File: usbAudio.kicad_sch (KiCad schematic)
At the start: 35 parts, among them J1 USB_B_Micro, J2 54-00176, U1 PCM2906CDBR, U2 MAX9814, U3 TCR2EF36, Y1 12MHz

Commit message: Update design and readme
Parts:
- removed C6: 1uF, Capacitor_SMD:C_0603_1608Metric_Pad1.08x0.95mm_HandSolder, symbol Device:C_Small
- removed D1: D_Schottky_Small, Diode_SMD:D_SOD-523, symbol Device:D_Schottky_Small
- removed JP1: Jumper_NC_Small, Jumper:SolderJumper-2_P1.3mm_Bridged_RoundedPad1.0x1.5mm, symbol Device:Jumper_NC_Small
- removed JP4: Jumper_NO_Small, Jumper:SolderJumper-2_P1.3mm_Open_RoundedPad1.0x1.5mm, symbol Device:Jumper_NO_Small
- removed R7: 13k, Resistor_SMD:R_0603_1608Metric_Pad0.98x0.95mm_HandSolder, symbol Device:R_Small_US
- removed R8: 27k, Resistor_SMD:R_0603_1608Metric_Pad0.98x0.95mm_HandSolder, symbol Device:R_Small_US
- removed U3: TCR2EF36, Package_TO_SOT_SMD:TSOT-23-5, symbol Regulator_Linear:ADP7142AUJZ-3.3
- added C1: 0.1uF, Capacitor_SMD:C_0603_1608Metric_Pad1.08x0.95mm_HandSolder, symbol Device:C_Small
- added C13, C16, C17: 1uF, Capacitor_SMD:C_0603_1608Metric_Pad1.08x0.95mm_HandSolder, symbol Device:C_Small
- added J2: Conn_01x03, Package_TO_SOT_THT:TO-92Flat, symbol Connector_Generic:Conn_01x03
- added U3: TCR2EF36, Package_TO_SOT_SMD:SOT-23-5, symbol Regulator_Linear:MIC5365-3.3YD5
- added U4: MIC5365-3.3YD5, Package_TO_SOT_SMD:SOT-23-5, symbol Regulator_Linear:MIC5365-3.3YD5
- renumbered C13 to C14, C14 to C15, C3 to C2, C8 to C3, C1 to C4, C2 to C6, C4 to C7, C7 to C8, J2 to J3, JP3 to JP1, R3 to R4, R4 to R5, R5 to R6, R2 to R7, R6 to R8
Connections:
- net AMPOUT: now also C1.2
- net GND: now also C13.2, C16.2, C17.2, J2.2 (Pin_2), U3.2 (GND), U4.2 (GND)
- net VBUS: now also C13.1, U3.1 (VIN)
- net VCCCI: now also C16.1, J2.1 (Pin_1), U3.5 (VOUT), U4.1 (VIN)
- net at R8.1, U2.13 (MICBIAS): now also JP2.1; no longer R1.1
- net MICIN: no longer names the net of C2.1, U2.8 (MICIN)
- net MICIN: no longer JP2.1
- net SSPND* renamed *SSPND
- net *SSPND: now also U3.3 (EN), U4.3 (EN)
- new net: C1.1, U1.12 (VINL)
- new net IN_R: J2.3 (Pin_3), U1.13 (VINR)
- new net VBIAS: C17.1, JP2.2, R1.1, U4.5 (VOUT)
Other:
- note added: "Amplifier"
- note added: "Codec"
- note added: "Connectors"
- note added: "Power"
- moved on the sheet: C10, C11, C12, C14, C15, C2, C3, C4, C5, C6, C7, C8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

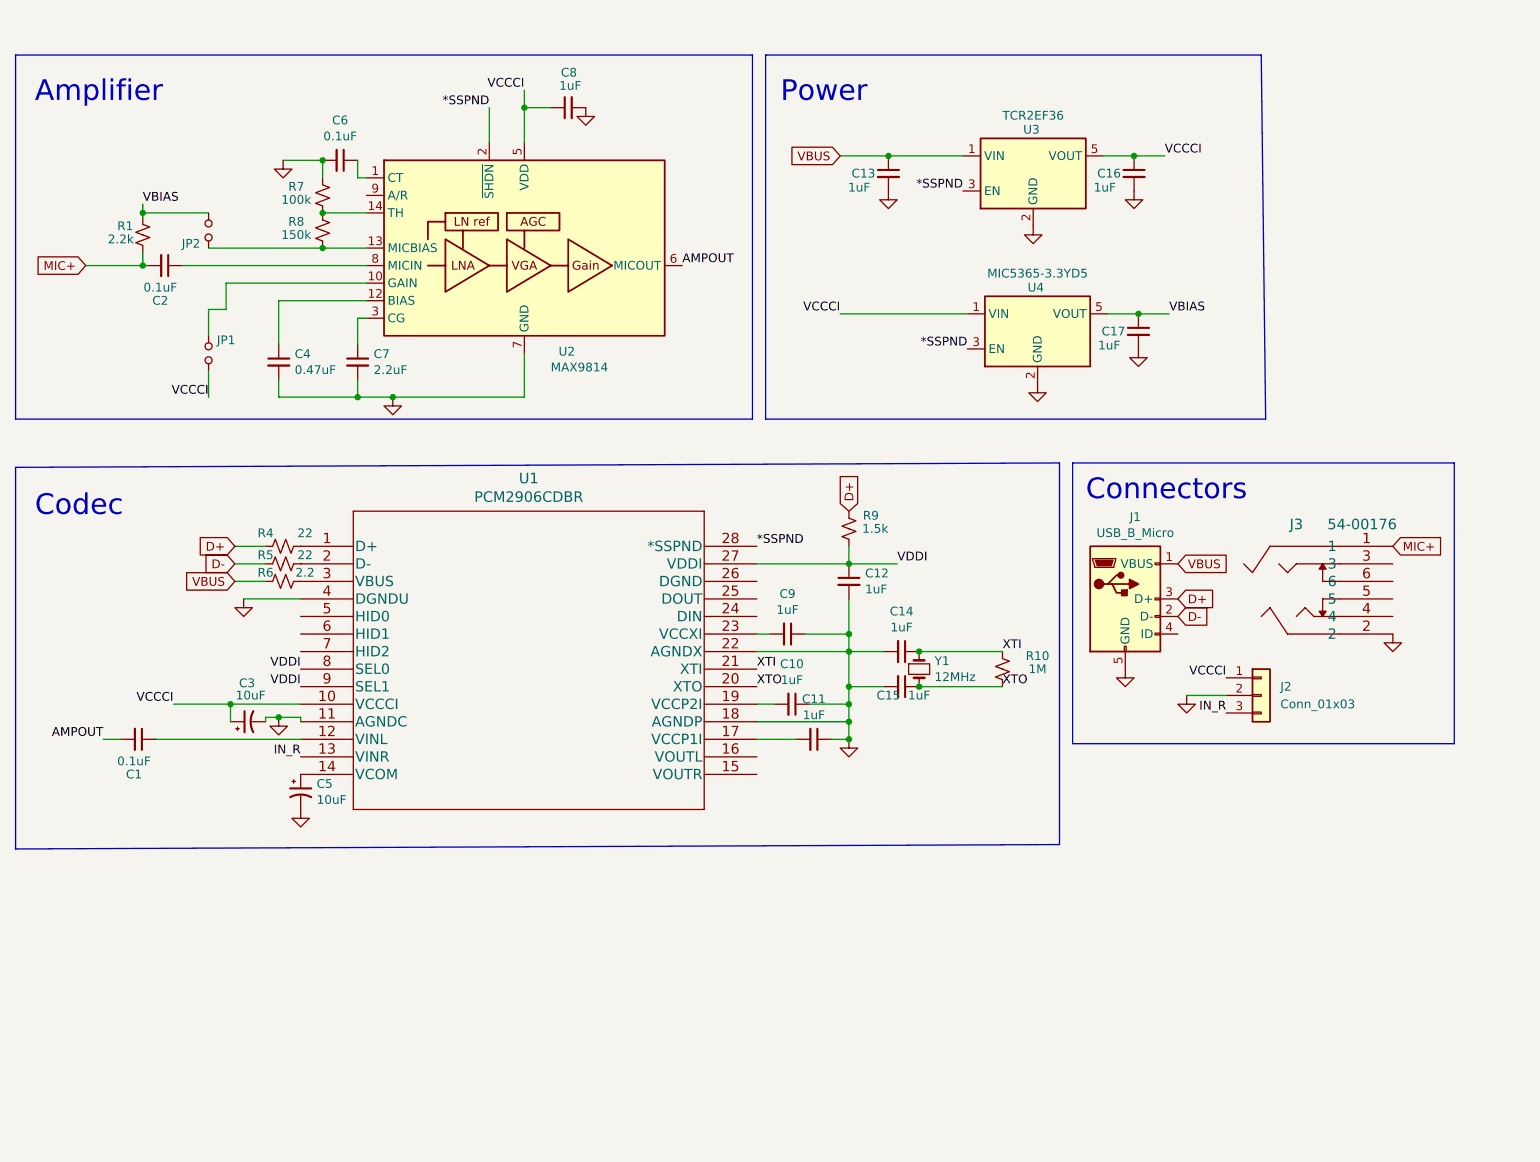
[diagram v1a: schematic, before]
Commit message: Updates from reddit feedback https://www.reddit.com/r/PrintedCircuitBoard/comments/so21cn/project_review_usb_microphone_interface/
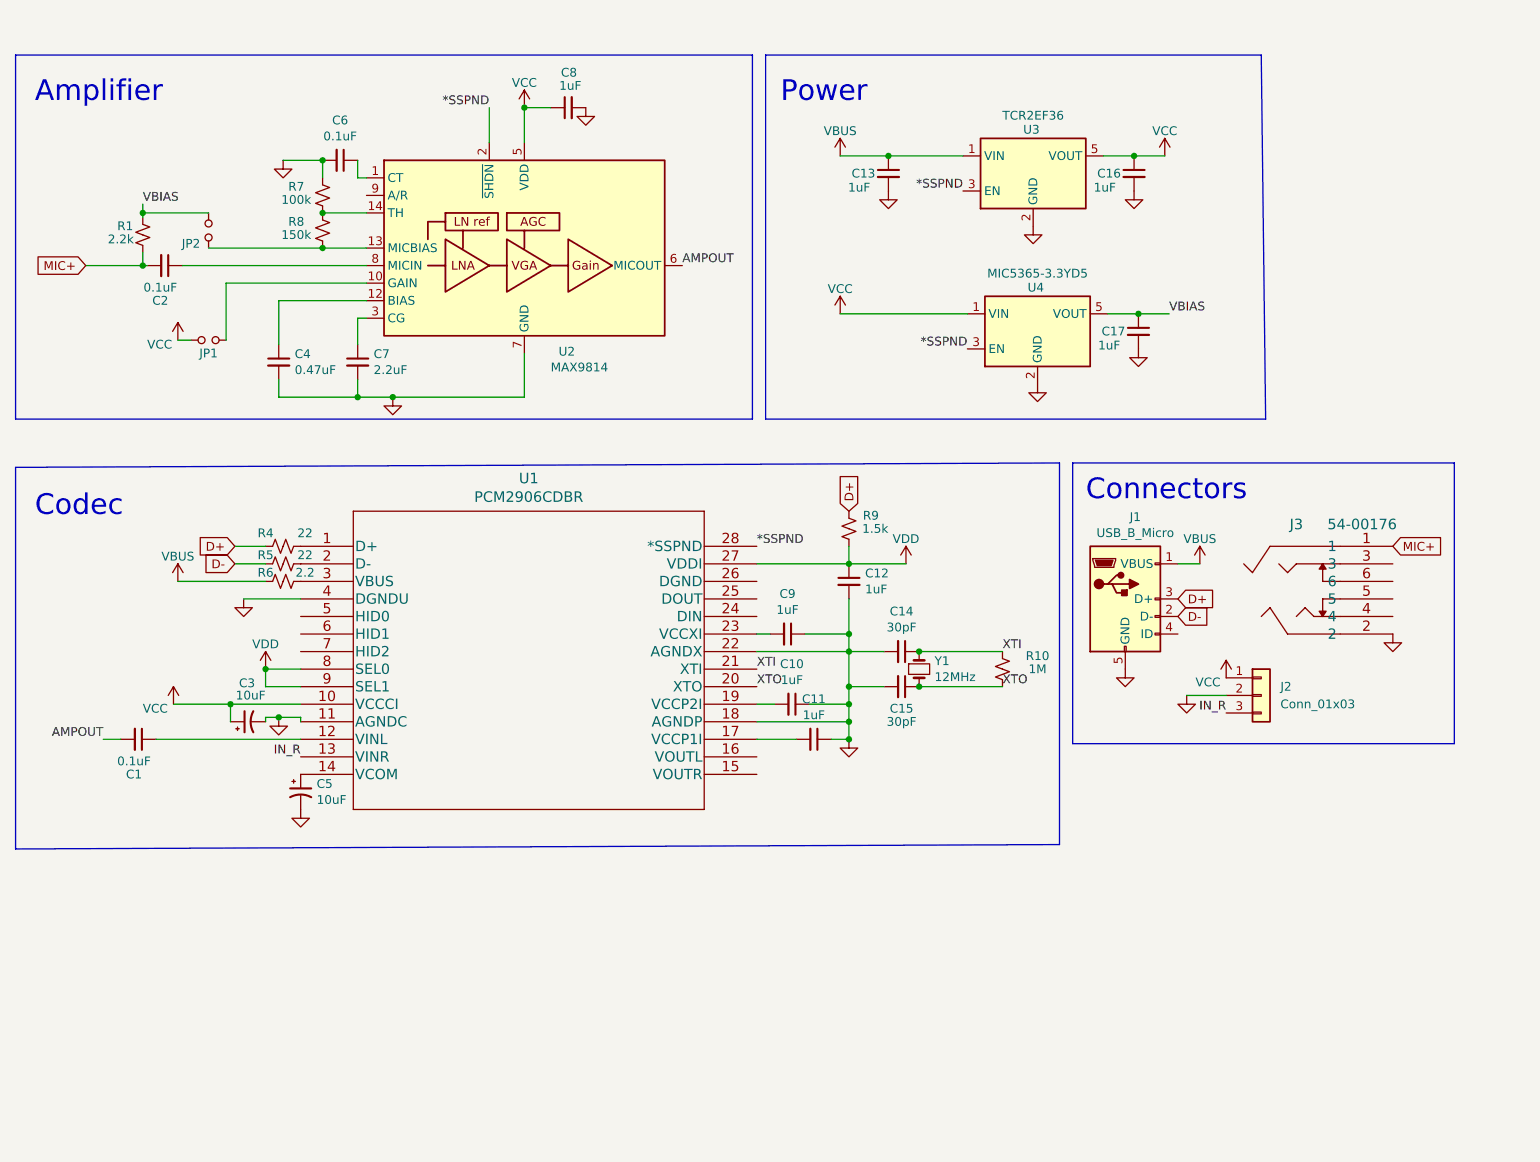
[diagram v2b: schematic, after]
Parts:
- C14, C15: value 1uF -> 30pF
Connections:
- net at U2.10 (GAIN): now also JP1.2; no longer JP1.1
- net VCCCI renamed VCC
- net VCC: now also JP1.1; no longer JP1.2
- net VDDI renamed VDD
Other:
- moved on the sheet: JP1

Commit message: Changes for JLC production. Add mounting hole.
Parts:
- U4: value MIC5365-3.3YD5 -> MIC5365-3.0YD5-TR
- Y1: footprint Crystal:Crystal_HC49-U_Vertical -> Crystal:Crystal_SMD_5032-4Pin_5.0x3.2mm
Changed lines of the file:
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@@
       (effects (font (size 1.27 1.27)) (justify left))
     )
-    (property "Footprint" "Crystal:Crystal_HC49-U_Vertical" (id 2) (at 153.67 109.22 0)
+    (property "Footprint" "Crystal:Crystal_SMD_5032-4Pin_5.0x3.2mm" (id 2) (at 153.67 109.22 0)
       (effects (font (size 1.27 1.27)) hide)
     )
@@
   (symbol (lib_id "power:VCC") (at 96.52 27.94 0) (unit 1)
     (in_bom yes) (on_board yes) (fields_autoplaced)
-    (property "Reference" "#PWR?" (id 0) (at 96.52 31.75 0)
+    (property "Reference" "#PWR0104" (id 0) (at 96.52 31.75 0)
       (effects (font (size 1.27 1.27)) hide)
     )
@@
   (symbol (lib_id "power:VDD") (at 59.055 109.22 0) (unit 1)
     (in_bom yes) (on_board yes) (fields_autoplaced)
-    (property "Reference" "#PWR?" (id 0) (at 59.055 113.03 0)
+    (property "Reference" "#PWR0108" (id 0) (at 59.055 113.03 0)
       (effects (font (size 1.27 1.27)) hide)
     )
@@
   (symbol (lib_id "power:VBUS") (at 46.355 96.52 0) (unit 1)
     (in_bom yes) (on_board yes) (fields_autoplaced)
-    (property "Reference" "#PWR?" (id 0) (at 46.355 100.33 0)
+    (property "Reference" "#PWR0106" (id 0) (at 46.355 100.33 0)
       (effects (font (size 1.27 1.27)) hide)
     )
@@
   (symbol (lib_id "power:VBUS") (at 194.31 93.98 0) (unit 1)
     (in_bom yes) (on_board yes) (fields_autoplaced)
-    (property "Reference" "#PWR?" (id 0) (at 194.31 97.79 0)
+    (property "Reference" "#PWR0109" (id 0) (at 194.31 97.79 0)
       (effects (font (size 1.27 1.27)) hide)
     )
@@
   (symbol (lib_id "power:VCC") (at 45.72 114.3 0) (unit 1)
     (in_bom yes) (on_board yes)
-    (property "Reference" "#PWR?" (id 0) (at 45.72 118.11 0)
+    (property "Reference" "#PWR0107" (id 0) (at 45.72 118.11 0)
       (effects (font (size 1.27 1.27)) hide)
     )
@@
   (symbol (lib_id "power:VCC") (at 198.12 110.49 0) (unit 1)
     (in_bom yes) (on_board yes)
-    (property "Reference" "#PWR?" (id 0) (at 198.12 114.3 0)
+    (property "Reference" "#PWR0110" (id 0) (at 198.12 114.3 0)
       (effects (font (size 1.27 1.27)) hide)
     )
@@
   (symbol (lib_id "power:VCC") (at 142.24 57.785 0) (unit 1)
     (in_bom yes) (on_board yes) (fields_autoplaced)
-    (property "Reference" "#PWR?" (id 0) (at 142.24 61.595 0)
+    (property "Reference" "#PWR0102" (id 0) (at 142.24 61.595 0)
       (effects (font (size 1.27 1.27)) hide)
     )
@@
   (symbol (lib_id "power:VCC") (at 46.355 61.595 0) (unit 1)
     (in_bom yes) (on_board yes)
-    (property "Reference" "#PWR?" (id 0) (at 46.355 65.405 0)
+    (property "Reference" "#PWR0105" (id 0) (at 46.355 65.405 0)
       (effects (font (size 1.27 1.27)) hide)
     )
@@
   (symbol (lib_id "power:VDD") (at 151.765 93.98 0) (unit 1)
     (in_bom yes) (on_board yes) (fields_autoplaced)
-    (property "Reference" "#PWR?" (id 0) (at 151.765 97.79 0)
+    (property "Reference" "#PWR0111" (id 0) (at 151.765 97.79 0)
       (effects (font (size 1.27 1.27)) hide)
     )
@@
   (symbol (lib_id "power:VCC") (at 189.23 34.925 0) (unit 1)
     (in_bom yes) (on_board yes) (fields_autoplaced)
-    (property "Reference" "#PWR?" (id 0) (at 189.23 38.735 0)
+    (property "Reference" "#PWR0101" (id 0) (at 189.23 38.735 0)
       (effects (font (size 1.27 1.27)) hide)
     )
@@
   (symbol (lib_id "power:VBUS") (at 142.24 34.925 0) (unit 1)
     (in_bom yes) (on_board yes) (fields_autoplaced)
-    (property "Reference" "#PWR?" (id 0) (at 142.24 38.735 0)
+    (property "Reference" "#PWR0103" (id 0) (at 142.24 38.735 0)
       (effects (font (size 1.27 1.27)) hide)
     )
@@
     (in_bom yes) (on_board yes)
     (property "Reference" "U4" (id 0) (at 170.561 53.975 0))
-    (property "Value" "MIC5365-3.3YD5" (id 1) (at 170.815 51.943 0))
+    (property "Value" "MIC5365-3.0YD5-TR" (id 1) (at 170.815 51.943 0))
     (property "Footprint" "Package_TO_SOT_SMD:SOT-23-5" (id 2) (at 170.815 51.435 0)
       (effects (font (size 1.27 1.27)) hide)
@@
       (reference "#PWR016") (unit 1) (value "GND") (footprint "")
     )
+    (path "/c5b1cfac-1d9a-444e-bca2-2f9eaff7e5f3"
+      (reference "#PWR0101") (unit 1) (value "VCC") (footprint "")
+    )
+    (path "/9bda69d1-98ce-44e9-a390-3559add57b5d"
+      (reference "#PWR0102") (unit 1) (value "VCC") (footprint "")
+    )
+    (path "/d017562e-a40c-4f70-9f0a-b4ef26701ced"
+      (reference "#PWR0103") (unit 1) (value "VBUS") (footprint "")
+    )
     (path "/1728e7e2-a540-4cf5-beb7-d102f3de991e"
-      (reference "#PWR?") (unit 1) (value "VCC") (footprint "")
+      (reference "#PWR0104") (unit 1) (value "VCC") (footprint "")
+    )
+    (path "/9e31d665-1c9d-4785-954e-8a8768e4f03b"
+      (reference "#PWR0105") (unit 1) (value "VCC") (footprint "")
+    )
+    (path "/2dff4ca6-e901-4498-90c4-7cae7e74345d"
+      (reference "#PWR0106") (unit 1) (value "VBUS") (footprint "")
+    )
+    (path "/3ee9974c-02ab-4004-aa04-8bf33ee52a5e"
+      (reference "#PWR0107") (unit 1) (value "VCC") (footprint "")
     )
     (path "/181cf366-3852-4dd2-9aec-7747b23a8ca6"
-      (reference "#PWR?") (unit 1) (value "VDD") (footprint "")
-    )
-    (path "/2dff4ca6-e901-4498-90c4-7cae7e74345d"
-      (reference "#PWR?") (unit 1) (value "VBUS") (footprint "")
+      (reference "#PWR0108") (unit 1) (value "VDD") (footprint "")
     )
     (path "/39225e57-3999-432c-b84c-821f28430b73"
-      (reference "#PWR?") (unit 1) (value "VBUS") (footprint "")
-    )
-    (path "/3ee9974c-02ab-4004-aa04-8bf33ee52a5e"
-      (reference "#PWR?") (unit 1) (value "VCC") (footprint "")
+      (reference "#PWR0109") (unit 1) (value "VBUS") (footprint "")
     )
     (path "/534b96e3-0f18-42e8-8ace-658ab4a24da5"
-      (reference "#PWR?") (unit 1) (value "VCC") (footprint "")
-    )
-    (path "/9bda69d1-98ce-44e9-a390-3559add57b5d"
-      (reference "#PWR?") (unit 1) (value "VCC") (footprint "")
-    )
-    (path "/9e31d665-1c9d-4785-954e-8a8768e4f03b"
-      (reference "#PWR?") (unit 1) (value "VCC") (footprint "")
+      (reference "#PWR0110") (unit 1) (value "VCC") (footprint "")
     )
     (path "/bd43ae5c-e7d5-448d-8b65-89afe5436a6f"
-      (reference "#PWR?") (unit 1) (value "VDD") (footprint "")
-    )
-    (path "/c5b1cfac-1d9a-444e-bca2-2f9eaff7e5f3"
-      (reference "#PWR?") (unit 1) (value "VCC") (footprint "")
-    )
-    (path "/d017562e-a40c-4f70-9f0a-b4ef26701ced"
-      (reference "#PWR?") (unit 1) (value "VBUS") (footprint "")
+      (reference "#PWR0111") (unit 1) (value "VDD") (footprint "")
     )
     (path "/83fa3abc-7420-4f33-91f3-33a175d205e1"
@@
     )
     (path "/daae3521-ca2d-418b-bea2-5f079e2339a6"
-      (reference "U4") (unit 1) (value "MIC5365-3.3YD5") (footprint "Package_TO_SOT_SMD:SOT-23-5")
+      (reference "U4") (unit 1) (value "MIC5365-3.0YD5-TR") (footprint "Package_TO_SOT_SMD:SOT-23-5")
     )
     (path "/00000000-0000-0000-0000-000061efb5c7"
-      (reference "Y1") (unit 1) (value "12MHz") (footprint "Crystal:Crystal_HC49-U_Vertical")
-    )
-  )
+      (reference "Y1") (unit 1) (value "12MHz") (footprint "Crystal:Crystal_SMD_5032-4Pin_5.0x3.2mm")
+    )
+  )

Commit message: Fix crystal pin mappings (1 and 3 instead of 1 and 2)
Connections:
- net XTO: now also Y1.3; no longer Y1.2
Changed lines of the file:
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@@
   (symbol (lib_id "Device:Crystal_Small") (at 153.67 109.22 270) (unit 1)
     (in_bom yes) (on_board yes)
-    (property "Reference" "Y1" (id 0) (at 155.9052 108.0516 90)
+    (property "Reference" "Y1" (id 0) (at 151.13 110.49 0)
       (effects (font (size 1.27 1.27)) (justify left))
     )
-    (property "Value" "12MHz" (id 1) (at 155.9052 110.363 90)
+    (property "Value" "12MHz" (id 1) (at 148.59 110.49 0)
       (effects (font (size 1.27 1.27)) (justify left))
     )
-    (property "Footprint" "Crystal:Crystal_SMD_5032-4Pin_5.0x3.2mm" (id 2) (at 153.67 109.22 0)
+    (property "Footprint" "Crystal:Crystal_SMD_5032-4Pin_5.0x3.2mm" (id 2) (at 161.29 109.22 0)
       (effects (font (size 1.27 1.27)) hide)
     )
@@
     )
     (pin "1")
-    (pin "2")
+    (pin "3")
   )
   (symbol (lib_id "Device:R_Small_US") (at 165.735 109.22 180) (unit 1)
